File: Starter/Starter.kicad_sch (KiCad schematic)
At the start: 67 parts, among them J2 Speaker, J5 Conn_01x08_Pin, M1 Vibration Motor, Q1 2N2222, SW1 UP, SW2 LEFT, SW3 DOWN, SW4 RIGHT, U1 MPU-6050, U2 LP-MSPM0G3507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

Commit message: footprints added
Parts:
- H1, H2, H3, H4: footprint (none) -> ECE319K:MountingHole_4_40
- Q1: footprint (none) -> ECE319K:SOT95P240X120-3N
- U3: footprint (none) -> ECE319K:SO08
- U5: footprint (none) -> ECE319K:SOIC127P600X175-16N; Mouser # (none) -> 511-ULN2003D1013TR; Mouser Link (none) -> https://www.mouser.com/ProductDetail/STMicroelectronics/ULN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; Our datasheet (none) -> https://www.mouser.com/datasheet/2/389/uln2001-1852702.pdf
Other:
- note added: "Audio amplifier reference: https://www.snapeda.com/parts/MC34119/NXP%20Semiconductors/view-part/"
- note added: "Reference: https://www.snapeda.com/parts/ULN2003BDR/Texas%20Instruments/view-part/?company=UTAustin&amp;welcome=home&amp;ref=search&amp;t=ULN2003B"
- note added: "Transistor reference: https://www.snapeda.com/parts/MMBT2222A/Diotec%20Semiconductor/view-part/?ref=search&t=MMBT2222A"
- note added: "double checkout footprint pinout"
- note added: "footprint check"
- note added: "mounting hole footprint from ECE319K library"
- note added: "two solder pads; edit in layout"

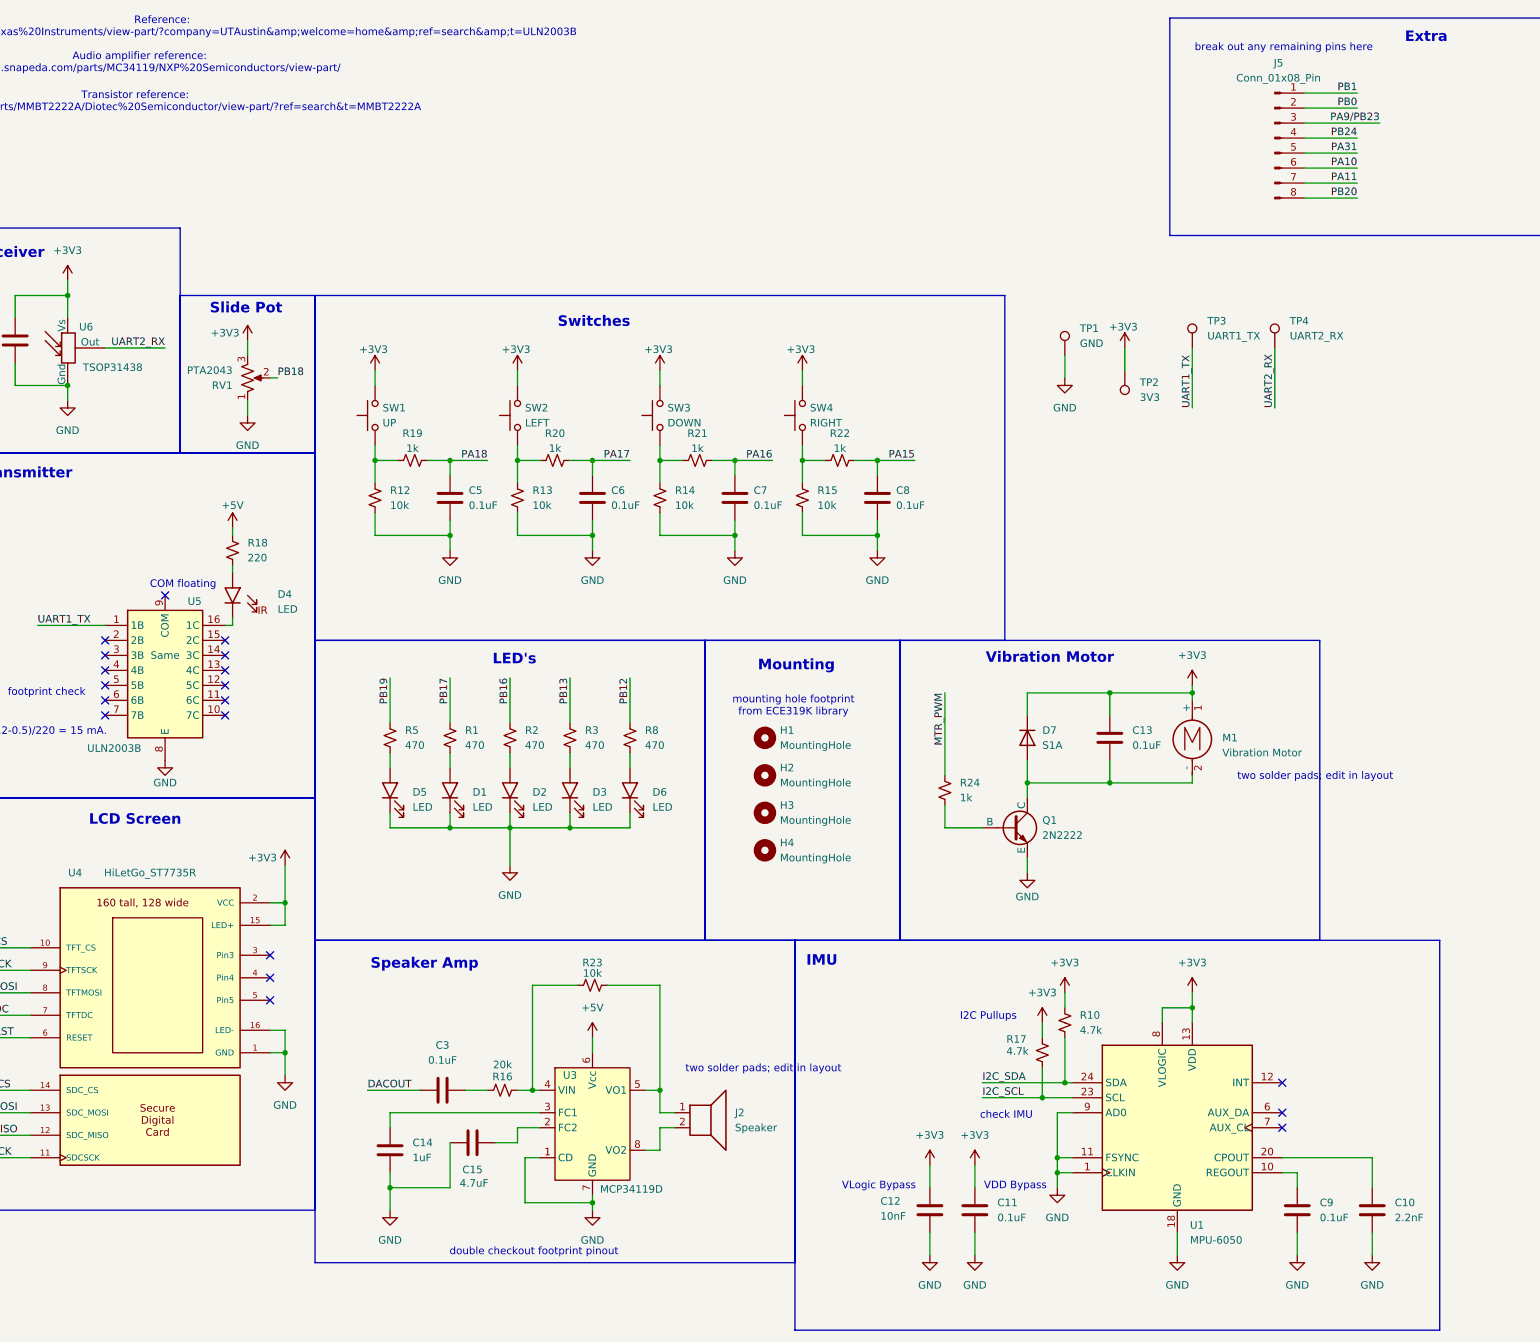
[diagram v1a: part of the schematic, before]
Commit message: Replaced IMU
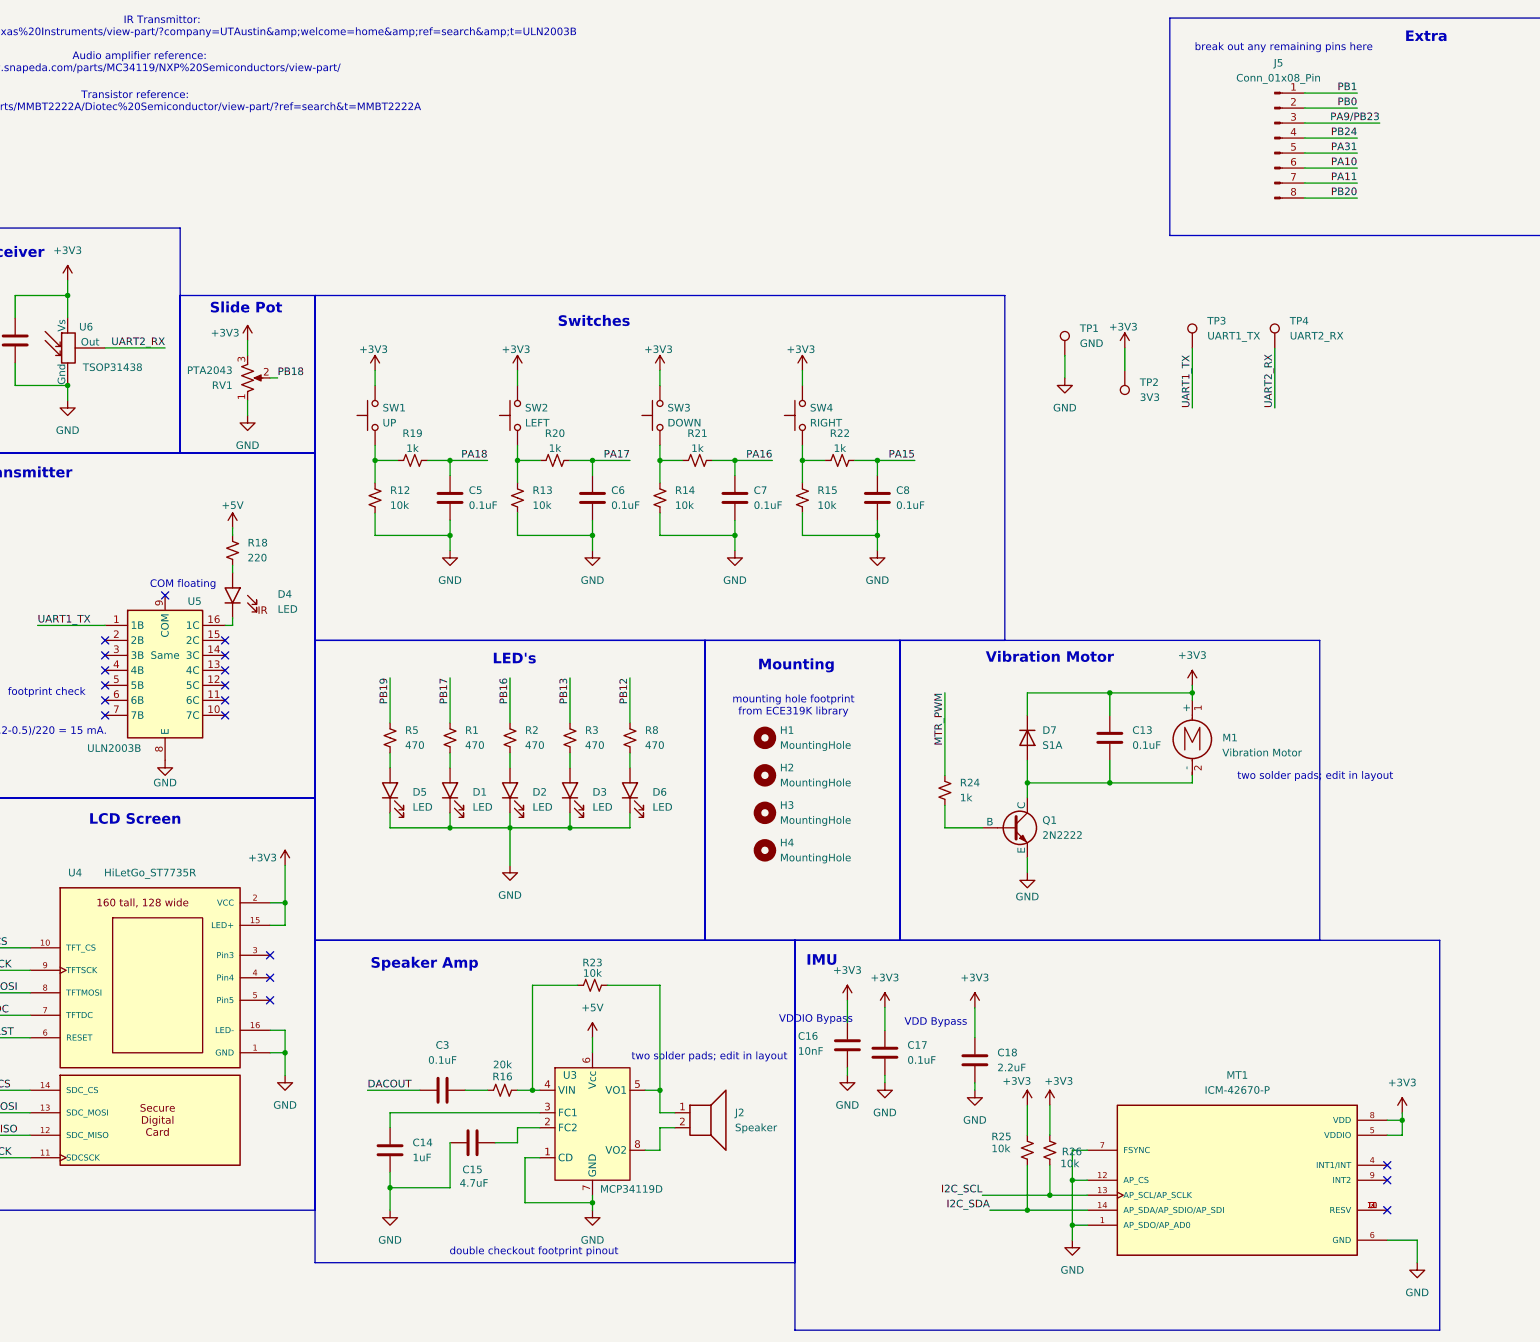
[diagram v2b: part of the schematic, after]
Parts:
- removed C10: 2.2nF, Capacitor_SMD:C_0603_1608Metric_Pad1.08x0.95mm_HandSolder, symbol ECE319K:C
- removed C11, C9: 0.1uF, Capacitor_SMD:C_0603_1608Metric_Pad1.08x0.95mm_HandSolder, symbol ECE319K:C
- removed C12: 10nF, Capacitor_SMD:C_0603_1608Metric_Pad1.08x0.95mm_HandSolder, symbol ECE319K:C
- removed R10, R17: 4.7k, Resistor_SMD:R_0603_1608Metric_Pad0.98x0.95mm_HandSolder, symbol ECE319K:R_0.125W
- removed U1: MPU-6050, Sensor_Motion:InvenSense_QFN-24_4x4mm_P0.5mm, symbol Sensor_Motion:MPU-6050
- added C16: 10nF, Capacitor_SMD:C_0603_1608Metric_Pad1.08x0.95mm_HandSolder, symbol ECE319K:C
- added C17: 0.1uF, Capacitor_SMD:C_0603_1608Metric_Pad1.08x0.95mm_HandSolder, symbol ECE319K:C
- added C18: 2.2uF, Capacitor_SMD:C_0603_1608Metric_Pad1.08x0.95mm_HandSolder, symbol ECE319K:C
- added MT1: ICM-42670-P, ECE319K:XDCR_ICM-42670-P, symbol ICM IMU:ICM-42670-P
- added R25, R26: 10k, Resistor_SMD:R_0603_1608Metric_Pad0.98x0.95mm_HandSolder, symbol ECE319K:R_0.125W
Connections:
- net +3V3: now also C16.1, C17.1, C18.1, MT1.5 (VDDIO), MT1.8 (VDD), R25.1, R26.1
- net GND: now also C16.2, C17.2, C18.2, MT1.1 (AP_SDO/AP_AD0), MT1.12 (AP_CS), MT1.6 (GND), MT1.7 (FSYNC)
- net I2C_SCL: now also MT1.13 (AP_SCL/AP_SCLK), R26.2
- net I2C_SDA: now also MT1.14 (AP_SDA/AP_SDIO/AP_SDI), R25.2
- new net: MT1.10 (RESV), MT1.11 (RESV), MT1.2 (RESV), MT1.3 (RESV)
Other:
- note added: "IR Transmittor: https://www.snapeda.com/parts/ULN2003BDR/Texas%20Instruments/view-part/?company=UTAustin&amp;welcome=home&amp;ref=search&amp;t=ULN2003B"
- note added: "VDDIO Bypass"
- note removed: "I2C Pullups"
- note removed: "Reference: https://www.snapeda.com/parts/ULN2003BDR/Texas%20Instruments/view-part/?company=UTAustin&amp;welcome=home&amp;ref=search&amp;t=ULN2003B"
- note removed: "VLogic Bypass"
- note removed: "check IMU"

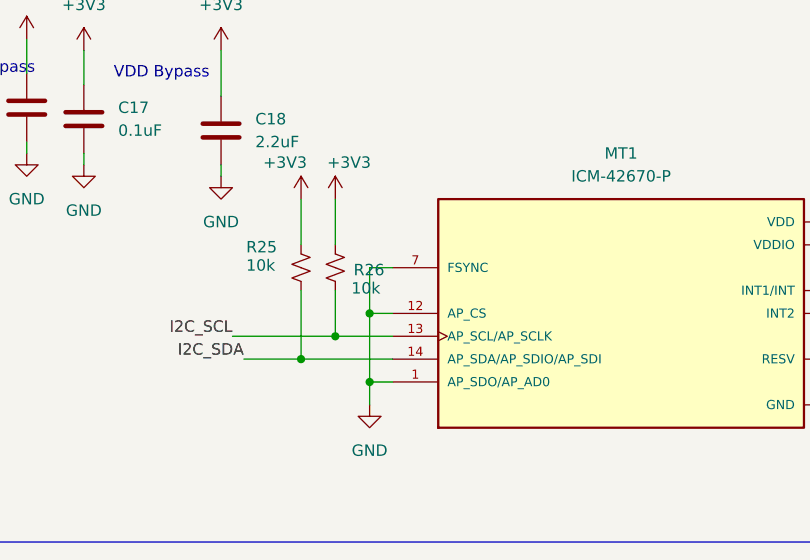
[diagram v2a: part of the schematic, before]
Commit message: THT additions
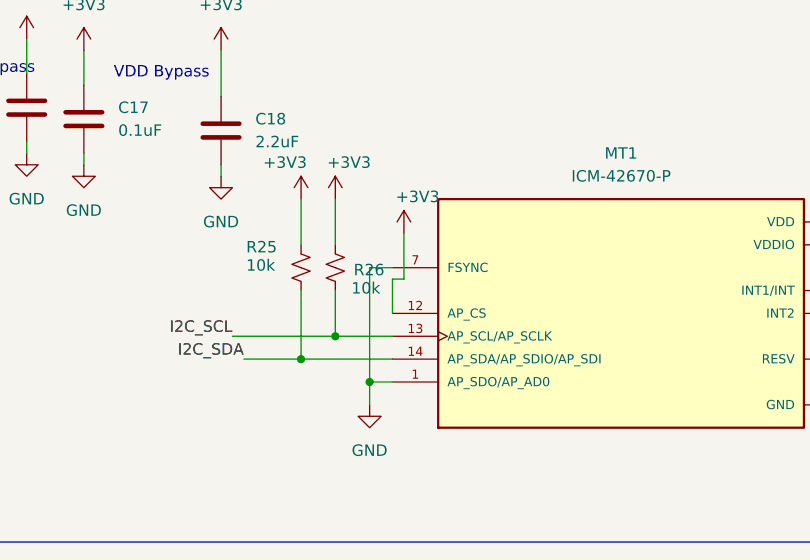
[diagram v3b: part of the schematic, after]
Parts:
- J2, M1: footprint Connector_Wire:SolderWirePad_1x01_SMD_1x2mm -> ECE319K:Testpoint_1x02_P2.54mm
- Q1: footprint ECE319K:SOT95P240X120-3N -> Package_TO_SOT_SMD:SOT-23
- SW1, SW2, SW3, SW4: footprint Button_Switch_SMD:SW_Push_1P1T_NO_6x6mm_H9.5mm -> Button_Switch_SMD:SW_SPST_PTS645; Mouser # 506-1977223-1 -> 506-1977223-1
- U3: footprint ECE319K:SO08 -> ECE319K:DIP-8_W7.62mm_LongPads
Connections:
- net +3V3: now also MT1.12 (AP_CS)
- net GND: no longer MT1.12 (AP_CS)
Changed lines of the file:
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@@
 	)
 	(junction
-		(at 313.69 212.09)
-		(diameter 0)
-		(color 0 0 0 0)
-	)
-	(junction
 		(at 143.51 77.47)
 		(diameter 0)
@@
 	(wire
 		(pts
-			(xy 313.69 212.09) (xy 313.69 219.71)
-		)
-		(stroke
-			(width 0)
-			(type default)
-		)
-	)
-	(wire
-		(pts
 			(xy 353.06 45.72) (xy 361.95 45.72)
 		)
@@
 	(wire
 		(pts
-			(xy 238.76 127) (xy 238.76 134.62)
+			(xy 316.23 208.28) (xy 317.5 208.28)
 		)
 		(stroke
@@
 	(wire
 		(pts
-			(xy 309.88 199.39) (xy 309.88 204.47)
+			(xy 238.76 127) (xy 238.76 134.62)
 		)
 		(stroke
@@
 	(wire
 		(pts
-			(xy 127 187.96) (xy 137.16 187.96)
+			(xy 309.88 199.39) (xy 309.88 204.47)
 		)
 		(stroke
@@
 	(wire
 		(pts
-			(xy 334.01 128.27) (xy 334.01 129.54)
+			(xy 127 187.96) (xy 137.16 187.96)
 		)
 		(stroke
@@
 	(wire
 		(pts
-			(xy 219.71 87.63) (xy 219.71 90.17)
+			(xy 334.01 128.27) (xy 334.01 129.54)
 		)
 		(stroke
@@
 	(wire
 		(pts
-			(xy 313.69 212.09) (xy 316.23 212.09)
+			(xy 219.71 87.63) (xy 219.71 90.17)
 		)
 		(stroke
@@
 	(wire
 		(pts
+			(xy 317.5 203.2) (xy 317.5 208.28)
+		)
+		(stroke
+			(width 0)
+			(type default)
+		)
+	)
+	(wire
+		(pts
 			(xy 104.14 184.15) (xy 104.14 194.31)
 		)
@@
 	(wire
 		(pts
-			(xy 313.69 207.01) (xy 313.69 212.09)
+			(xy 313.69 207.01) (xy 313.69 219.71)
 		)
 		(stroke
@@
 	(wire
 		(pts
+			(xy 316.23 212.09) (xy 316.23 208.28)
+		)
+		(stroke
+			(width 0)
+			(type default)
+		)
+	)
+	(wire
+		(pts
 			(xy 143.51 77.47) (xy 143.51 80.01)
 		)
@@
 			)
 		)
-		(property "Footprint" "Button_Switch_SMD:SW_Push_1P1T_NO_6x6mm_H9.5mm"
+		(property "Footprint" "Button_Switch_SMD:SW_SPST_PTS645"
 			(at 262.89 82.55 0)
 			(effects
@@
 			)
 		)
-		(property "Mouser #" "506-1977223-1 "
+		(property "Mouser #" "506-1977223-1"
 			(at 267.97 82.55 0)
 			(effects
@@
 			)
 		)
-		(property "Footprint" "Connector_Wire:SolderWirePad_1x01_SMD_1x2mm"
+		(property "Footprint" "ECE319K:Testpoint_1x02_P2.54mm"
 			(at 334.01 138.176 0)
 			(effects
@@
 			)
 		)
+		(property "JLCPCB #" ""
+			(at 334.01 135.89 0)
+			(effects
+				(font
+					(size 1.27 1.27)
+				)
+				(hide yes)
+			)
+		)
 		(pin "1"
 		)
@@
 			)
 		)
-		(property "Footprint" "Button_Switch_SMD:SW_Push_1P1T_NO_6x6mm_H9.5mm"
+		(property "Footprint" "Button_Switch_SMD:SW_SPST_PTS645"
 			(at 238.76 82.55 0)
 			(effects
@@
 			)
 		)
-		(property "Mouser #" "506-1977223-1 "
+		(property "Mouser #" "506-1977223-1"
 			(at 243.84 82.55 0)
 			(effects
@@
 			)
 		)
-		(property "Footprint" "ECE319K:SO08"
+		(property "Footprint" "ECE319K:DIP-8_W7.62mm_LongPads"
 			(at 232.41 191.77 0)
 			(effects
@@
 			)
 		)
-		(property "Footprint" "ECE319K:SOT95P240X120-3N"
+		(property "Footprint" "Package_TO_SOT_SMD:SOT-23"
 			(at 367.03 152.4 0)
 			(effects
@@
 			)
 		)
-		(property "Footprint" "Connector_Wire:SolderWirePad_1x01_SMD_1x2mm"
+		(property "Footprint" "ECE319K:Testpoint_1x02_P2.54mm"
 			(at 251.46 205.74 0)
 			(effects
@@
 			)
 		)
+		(property "Mouser Link" ""
+			(at 251.46 200.66 0)
+			(effects
+				(font
+					(size 1.27 1.27)
+				)
+				(hide yes)
+			)
+		)
+		(property "Mouser #" ""
+			(at 251.46 200.66 0)
+			(effects
+				(font
+					(size 1.27 1.27)
+				)
+				(hide yes)
+			)
+		)
+		(property "JLCPCB #" ""
+			(at 251.46 200.66 0)
+			(effects
+				(font
+					(size 1.27 1.27)
+				)
+				(hide yes)
+			)
+		)
 		(pin "1"
 		)
@@
 			)
 		)
-		(property "Footprint" "Button_Switch_SMD:SW_Push_1P1T_NO_6x6mm_H9.5mm"
+		(property "Footprint" "Button_Switch_SMD:SW_SPST_PTS645"
 			(at 190.5 82.55 0)
 			(effects
@@
 			)
 		)
-		(property "Mouser #" "506-1977223-1 "
+		(property "Mouser #" "506-1977223-1"
 			(at 195.58 82.55 0)
 			(effects
@@
 	)
 	(symbol
+		(lib_id "power:+3V3")
+		(at 317.5 203.2 0)
+		(unit 1)
+		(exclude_from_sim no)
+		(in_bom yes)
+		(on_board yes)
+		(dnp no)
+		(property "Reference" "#PWR0126"
+			(at 317.5 207.01 0)
+			(effects
+				(font
+					(size 1.27 1.27)
+				)
+				(hide yes)
+			)
+		)
+		(property "Value" "+3V3"
+			(at 319.024 199.136 0)
+			(effects
+				(font
+					(size 1.27 1.27)
+				)
+			)
+		)
+		(property "Footprint" ""
+			(at 317.5 203.2 0)
+			(effects
+				(font
+					(size 1.27 1.27)
+				)
+				(hide yes)
+			)
+		)
+		(property "Datasheet" ""
+			(at 317.5 203.2 0)
+			(effects
+				(font
+					(size 1.27 1.27)
+				)
+				(hide yes)
+			)
+		)
+		(property "Description" ""
+			(at 317.5 203.2 0)
+			(effects
+				(font
+					(size 1.27 1.27)
+				)
+			)
+		)
+		(pin "1"
+		)
+		(instances
+			(project "Starter"
+				(path "/69b823fd-c065-40ff-9bb9-c5835555f3eb"
+					(reference "#PWR0126")
+					(unit 1)
+				)
+			)
+		)
+	)
+	(symbol
 		(lib_id "ECE319K:R_0.125W")
 		(at 195.58 96.52 0)
@@
 			)
 		)
-		(property "Footprint" "Button_Switch_SMD:SW_Push_1P1T_NO_6x6mm_H9.5mm"
+		(property "Footprint" "Button_Switch_SMD:SW_SPST_PTS645"
 			(at 214.63 82.55 0)
 			(effects
@@
 			)
 		)
-		(property "Mouser #" "506-1977223-1 "
+		(property "Mouser #" "506-1977223-1"
 			(at 219.71 82.55 0)
 			(effects

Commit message: initial layout
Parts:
- removed TP1: GND, TestPoint:TestPoint_Pad_1.0x1.0mm, symbol Connector:TestPoint
- removed TP2: 3V3, TestPoint:TestPoint_Pad_1.0x1.0mm, symbol Connector:TestPoint
- removed TP3: UART1_TX, TestPoint:TestPoint_Pad_1.0x1.0mm, symbol Connector:TestPoint
- removed TP4: UART2_RX, TestPoint:TestPoint_Pad_1.0x1.0mm, symbol Connector:TestPoint
- D4: footprint LED_SMD:LED_0805_2012Metric -> ECE319K:LED_D5.0mm
- H1, H2, H3, H4: footprint ECE319K:MountingHole_4_40 -> MountingHole:MountingHole_3.2mm_M3
